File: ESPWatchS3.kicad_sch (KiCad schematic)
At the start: 132 parts, among them J1 USB, J2 OLED, J3 UART0, Q1 DMN2050LFDB, SW1 Reset, SW2 Boot, SW3 User 1, SW4 User 2, SW5 User 3, SW6 User 4, U1 ESP32-S3R8, U10 BD48KxxG, U11 NJG1143UA2-TE1, U2 EVA-M8Q-0, U3 BME280, U4 TPS631000DRLR, U5 AP3012, U6 BQ298012, U7 BQ27441-G1A, U8 BQ24075RGTR, U9 IS25LP128F-JKLE, Y1 40MHz, Y2 32.768kHz, Y3 32.768kHz

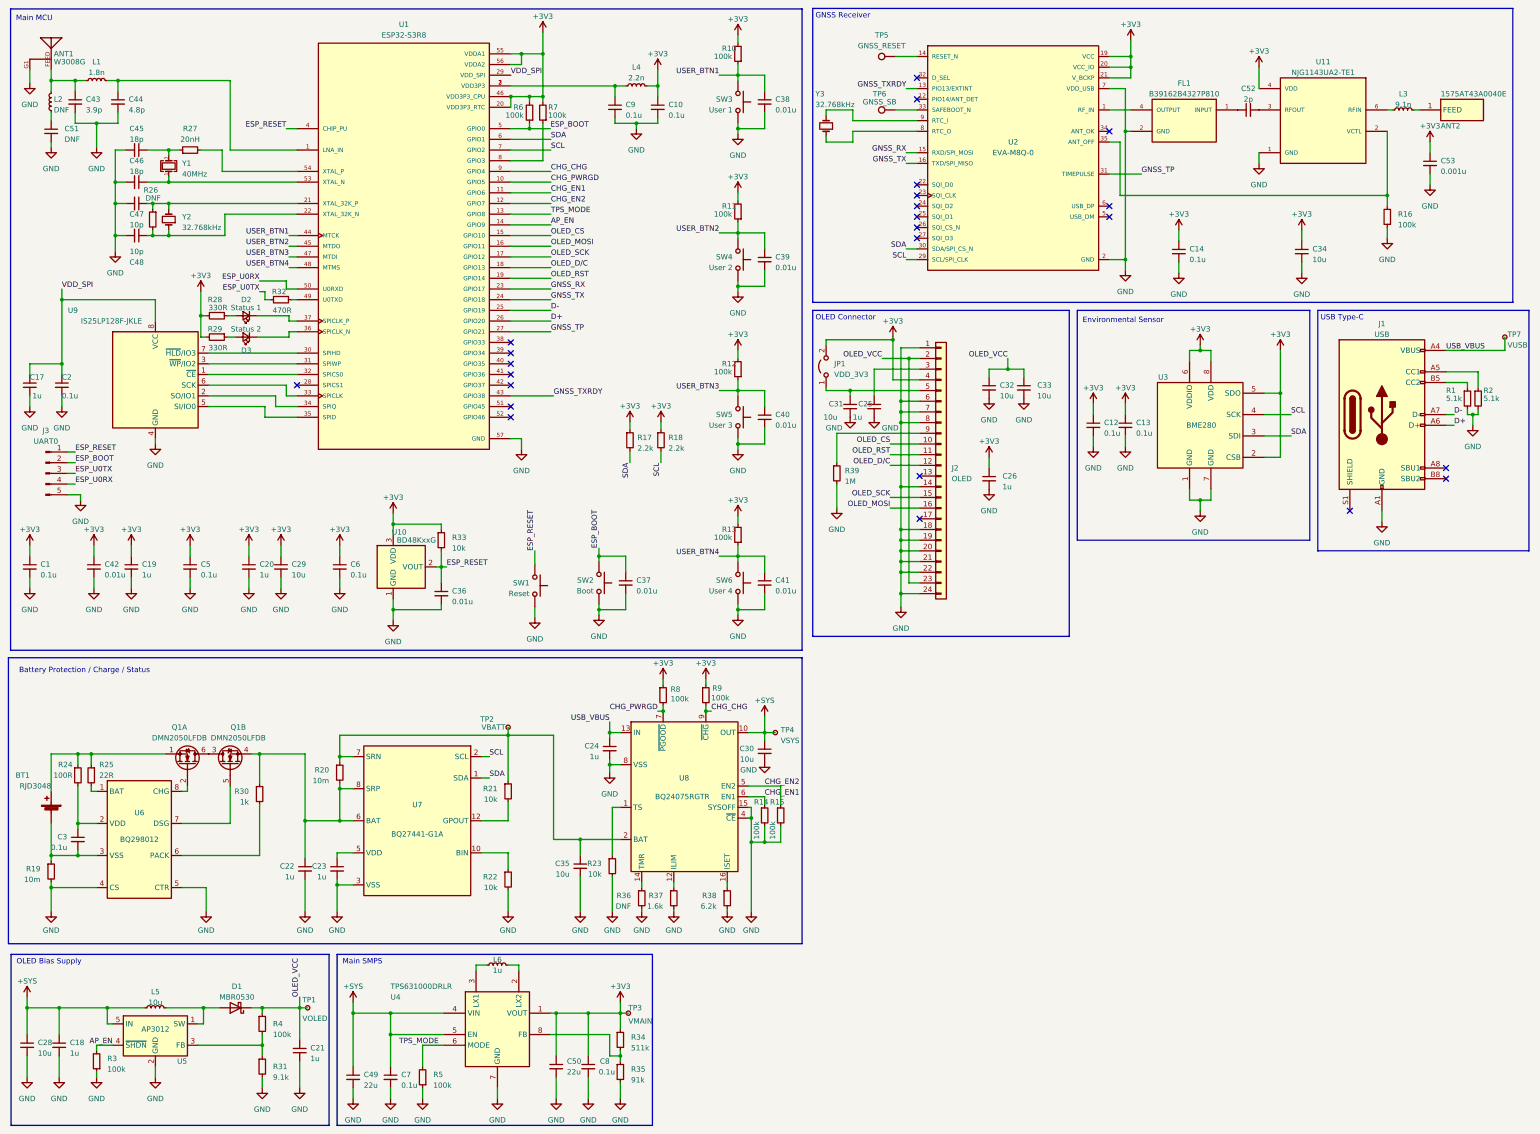
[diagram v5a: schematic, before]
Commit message: Update schematic with V1.0 design
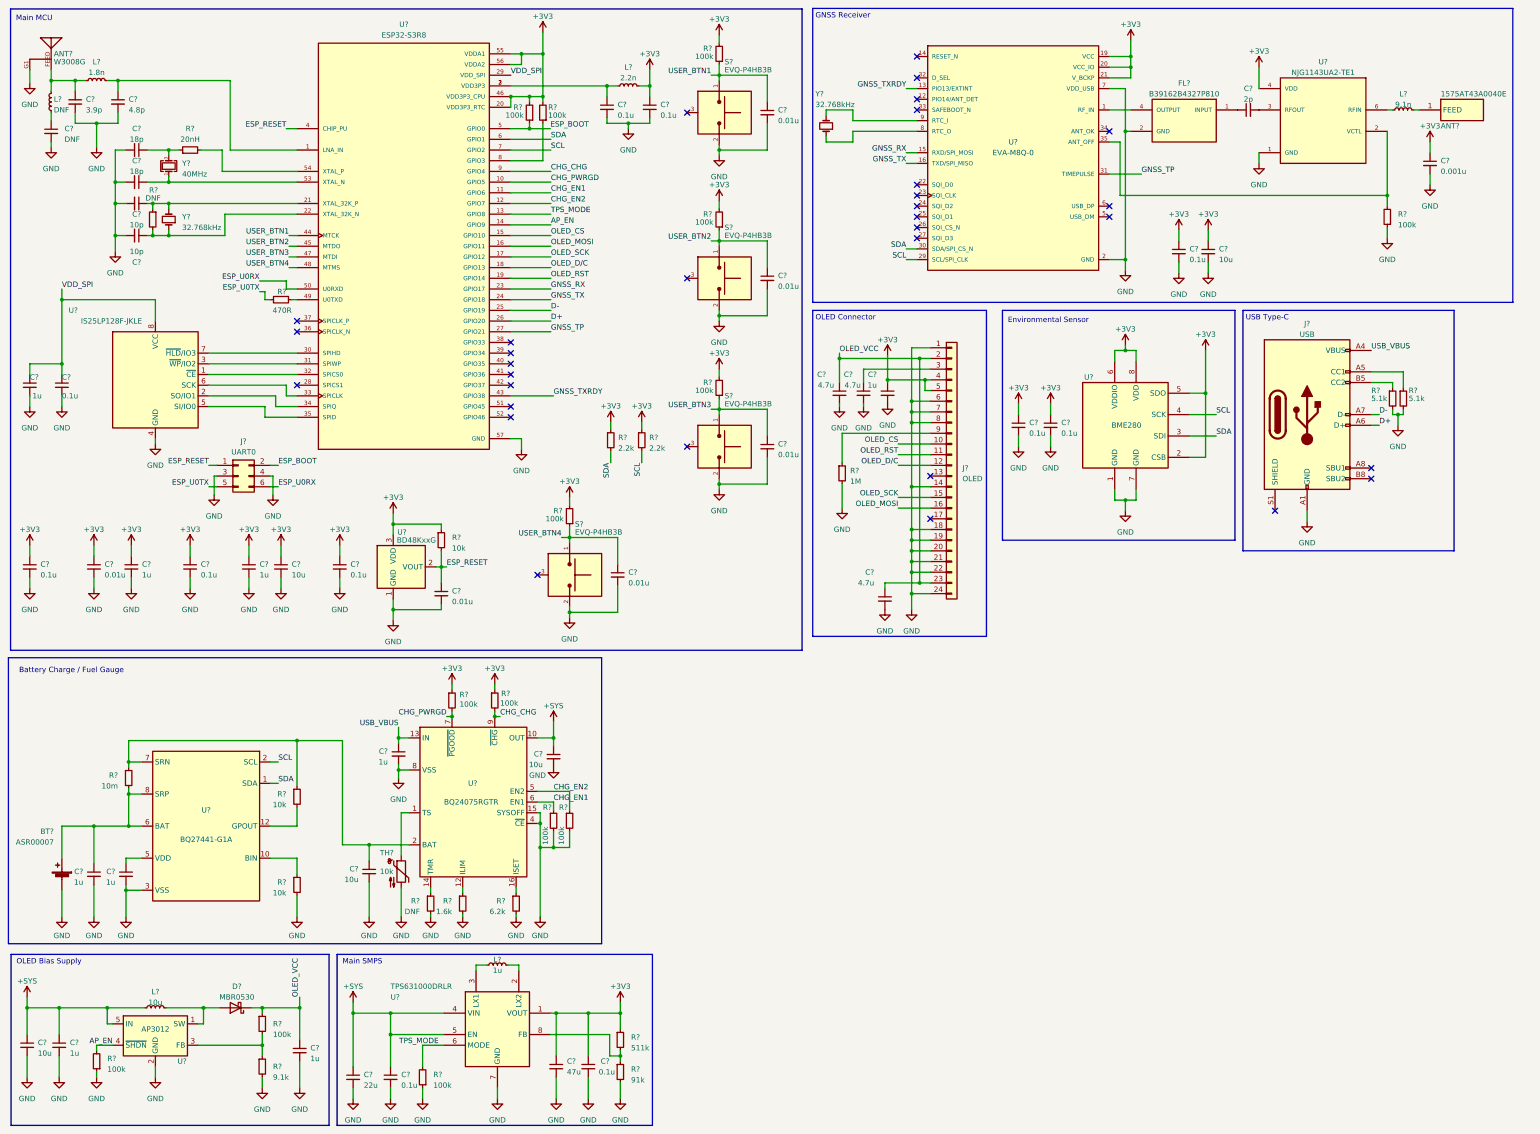
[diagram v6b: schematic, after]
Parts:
- removed BT1: RJD3048, WatchParts:BAT_3046, symbol Device:Battery_Cell
- removed C25, C26: 1u, Capacitor_SMD:C_0603_1608Metric, symbol Device:C_Small
- removed C3: 0.1u, Capacitor_SMD:C_0402_1005Metric, symbol Device:C_Small
- removed C31, C32, C33, C34: 10u, Capacitor_SMD:C_0805_2012Metric, symbol Device:C_Small
- removed C37, C39, C40, C41: 0.01u, Capacitor_SMD:C_0402_1005Metric, symbol Device:C_Small
- removed D2: Status 1, LED_SMD:LED_0603_1608Metric, symbol Device:LED_Small
- removed D3: Status 2, LED_SMD:LED_0603_1608Metric, symbol Device:LED_Small
- removed J3: UART0, Connector_PinHeader_2.54mm:PinHeader_1x05_P2.54mm_Vertical, symbol Connector:Conn_01x05_Pin
- removed JP1: VDD_3V3, Jumper:SolderJumper-2_P1.3mm_Open_RoundedPad1.0x1.5mm, symbol Jumper:Jumper_2_Open
- removed Q1: DMN2050LFDB, WatchParts:MOSFET_DMP2160UFDB-7, symbol WatchParts:DMN2050LFDB
- removed R11, R12, R13: 100k, Resistor_SMD:R_0402_1005Metric, symbol Device:R_Small
- removed R19: 10m, Resistor_SMD:R_0805_2012Metric, symbol Device:R_Small
- removed R23: 10k, Resistor_SMD:R_0402_1005Metric, symbol Device:R_Small
- removed R24: 100R, Resistor_SMD:R_0402_1005Metric, symbol Device:R_Small
- removed R25: 22R, Resistor_SMD:R_0402_1005Metric, symbol Device:R_Small
- removed R28, R29: 330R, Resistor_SMD:R_0402_1005Metric, symbol Device:R_Small
- removed R30: 1k, Resistor_SMD:R_0402_1005Metric, symbol Device:R_Small
- removed SW1: Reset, WatchParts:PTS815SJM250SMTRLFS, symbol WatchParts:PTS815
- removed SW2: Boot, WatchParts:PTS815SJM250SMTRLFS, symbol WatchParts:PTS815
- removed SW3: User 1, WatchParts:PTS815SJM250SMTRLFS, symbol WatchParts:PTS815
- removed SW4: User 2, WatchParts:PTS815SJM250SMTRLFS, symbol WatchParts:PTS815
- removed SW5: User 3, WatchParts:PTS815SJM250SMTRLFS, symbol WatchParts:PTS815
- removed SW6: User 4, WatchParts:PTS815SJM250SMTRLFS, symbol WatchParts:PTS815
- removed TP1: VOLED, TestPoint:TestPoint_Pad_D1.5mm, symbol Connector:TestPoint_Small
- removed TP2: VBATT, TestPoint:TestPoint_Pad_D1.5mm, symbol Connector:TestPoint_Small
- removed TP3: VMAIN, TestPoint:TestPoint_Pad_D1.5mm, symbol Connector:TestPoint_Small
- removed TP4: VSYS, TestPoint:TestPoint_Pad_D1.5mm, symbol Connector:TestPoint_Small
- removed TP5: GNSS_RESET, TestPoint:TestPoint_Pad_D1.5mm, symbol Connector:TestPoint
- removed TP6: GNSS_SB, TestPoint:TestPoint_Pad_D1.5mm, symbol Connector:TestPoint
- removed TP7: VUSB, TestPoint:TestPoint_Pad_D1.5mm, symbol Connector:TestPoint_Small
- removed U6: BQ298012, WatchParts:QFN50P150X150X40-8N, symbol WatchParts:BQ298012RUGR
- added BT?: ASR00007, Connector_JST:JST_SH_SM02B-SRSS-TB_1x02-1MP_P1.00mm_Horizontal, symbol Device:Battery_Cell
- added C? (x3): 4.7u, symbol Device:C_Small
- added C?: 1u, symbol Device:C_Small
- added C? (x3): 0.01u, Capacitor_SMD:C_0402_1005Metric, symbol Device:C_Small
- added C?: 10u, Capacitor_SMD:C_0402_1005Metric, symbol Device:C_Small
- added J?: UART0, symbol Connector_Generic:Conn_02x03_Odd_Even
- added R? (x3): 100k, Resistor_SMD:R_0402_1005Metric, symbol Device:R_Small
- added S? (x4): EVQ-P4HB3B, WatchParts:SW_EVQ-P4HB3B, symbol WatchParts:EVQ-P4HB3B
- added TH?: 10k, symbol Device:Thermistor_NTC
- C?: renamed from C50; value 22u -> 47u
- renumbered ANT1 to ANT?, ANT2 to ANT?, C44 to C?, C20 to C?, C8 to C?, C48 to C?, C9 to C?, C49 to C?, C46 to C?, C22 to C?, C7 to C?, C6 to C?, C24 to C?, C23 to C?, C10 to C?, C19 to C?, C51 to C?, C30 to C?, C52 to C?, C5 to C?, C43 to C?, C18 to C?, C13 to C?, C29 to C?, C12 to C?, C35 to C?, C1 to C?, C28 to C?, C42 to C?, C38 to C?, C17 to C?, C14 to C?, C53 to C?, C47 to C?, C21 to C?, C45 to C?, C36 to C?, C2 to C?, D1 to D?, FL1 to FL?, J1 to J?, J2 to J?, L2 to L?, L6 to L?, L3 to L?, L5 to L?, L1 to L?, L4 to L?, R4 to R?, R8 to R?, R21 to R?, R33 to R?, R20 to R?, R18 to R?, R1 to R?, R38 to R?, R6 to R?, R27 to R?, R22 to R?, R15 to R?, R37 to R?, R31 to R?, R7 to R?, R5 to R?, R17 to R?, R34 to R?, R26 to R?, R14 to R?, R35 to R?, R9 to R?, R2 to R?, R16 to R?, R3 to R?, R36 to R?, R39 to R?, R10 to R?, R32 to R?, U2 to U?, U3 to U?, U1 to U?, U5 to U?, U7 to U?, U4 to U?, U10 to U?, U11 to U?, U9 to U?, U8 to U?, Y1 to Y?, Y3 to Y?, Y2 to Y?
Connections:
- net +3V3: now also J?.5 (Pin_5), C?.1, C?.1, R?.2, R?.2, R?.2
- net EP: now also BT?.2 (-), C?.2, C?.2, C?.2, C?.2, C?.2, C?.2, C?.2, C?.2, J?.3 (Pin_3), J?.4 (Pin_4), S?.2, S?.2, S?.2, S?.2, TH?.2
- net ESP_BOOT: now also J?.2 (Pin_2)
- net ESP_RESET: now also J?.1 (Pin_1)
- net ESP_U0RX: now also J?.6 (Pin_6)
- net ESP_U0TX: now also J?.5 (Pin_5)
- net OLED_VCC: now also C?.1, C?.1
- net USER_BTN1: now also S?.1
- net USER_BTN2: now also C?.1, R?.1, S?.1
- net USER_BTN3: now also C?.1, R?.1, S?.1
- net USER_BTN4: now also C?.1, R?.1, S?.1
- net at J?.3 (Pin_3): now also C?.1
- net at C?.1, R?.2, U?.6 (BAT)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: now also BT?.1 (+)
- net at U?.1 (TS): now also TH?.1
- new net: S?.3, S?.4 (x4)
- no-connect marks 24 -> 32
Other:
- note added: "Battery Charge / Fuel Gauge"
- note removed: "Battery Protection / Charge / Status"
- moved on the sheet: C?, J?, L?, R?, U?

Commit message: Finish reannotation of schematic
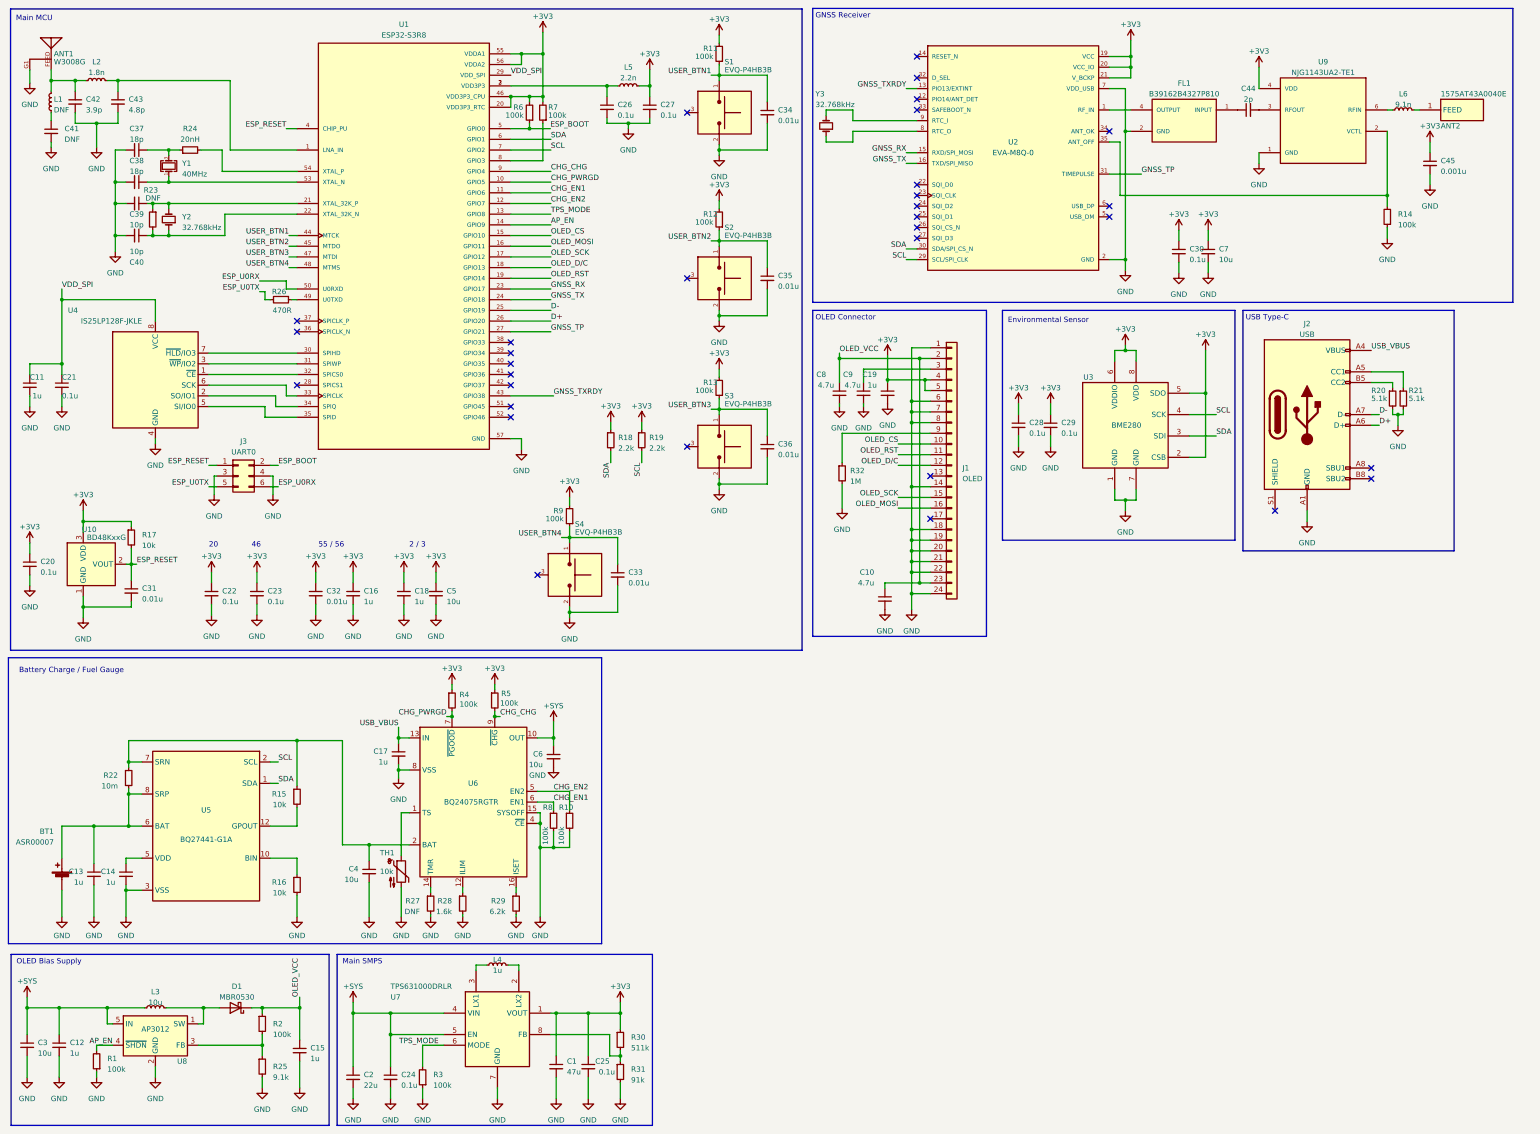
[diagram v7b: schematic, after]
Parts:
- C10, C8, C9: renamed from C?; footprint (none) -> Capacitor_SMD:C_0603_1608Metric
- C11, C12, C13, C14, C15, C16, C17, C18: renamed from C?; footprint Capacitor_SMD:C_0603_1608Metric -> Capacitor_SMD:C_0402_1005Metric
- C19: renamed from C?; footprint (none) -> Capacitor_SMD:C_0402_1005Metric
- C2: renamed from C?; footprint Capacitor_SMD:C_0805_2012Metric -> Capacitor_SMD:C_0603_1608Metric
- C3, C4, C5, C6: renamed from C?; footprint Capacitor_SMD:C_0805_2012Metric -> Capacitor_SMD:C_0402_1005Metric
- J3: renamed from J?; footprint (none) -> Connector:Tag-Connect_TC2030-IDC-NL_2x03_P1.27mm_Vertical
- TH1: renamed from TH?; footprint (none) -> Resistor_SMD:R_0603_1608Metric
- gave numbers to parts that had none: 90
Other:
- note added: "2 / 3"
- note added: "20"
- note added: "46"
- note added: "55 / 56"
- moved on the sheet: C16, C18, C20, C22, C23, C31, C32, C5, R17, U10
